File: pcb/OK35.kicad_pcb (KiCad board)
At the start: 2 copper layers, 133.3 x 116.2 mm, 78 parts, among them SW1 SW_SPST, SW10 SW_SPST, SW11 SW_SPST, SW12 SW_SPST, SW13 SW_SPST, SW14 SW_SPST, SW15 SW_SPST, SW16 SW_SPST, SW17 SW_SPST, SW18 SW_SPST, SW19 SW_SPST, SW2 SW_SPST, SW20 SW_SPST, SW21 SW_SPST, SW22 SW_SPST, SW23 SW_SPST, SW24 SW_SPST, SW25 SW_SPST, SW26 SW_SPST, SW27 SW_SPST, SW28 SW_SPST, SW29 SW_SPST, SW3 SW_SPST, SW30 SW_SPST, SW31 SW_SPST, SW32 SW_SPST, SW33 SW_SPST, SW34 SW_SPST, SW35 SW_SPST, SW4 SW_SPST, SW5 SW_SPST, SW6 SW_SPST, SW7 SW_SPST, SW8 SW_SPST, SW9 SW_SPST, U1 TRRS, U2 ProMicro

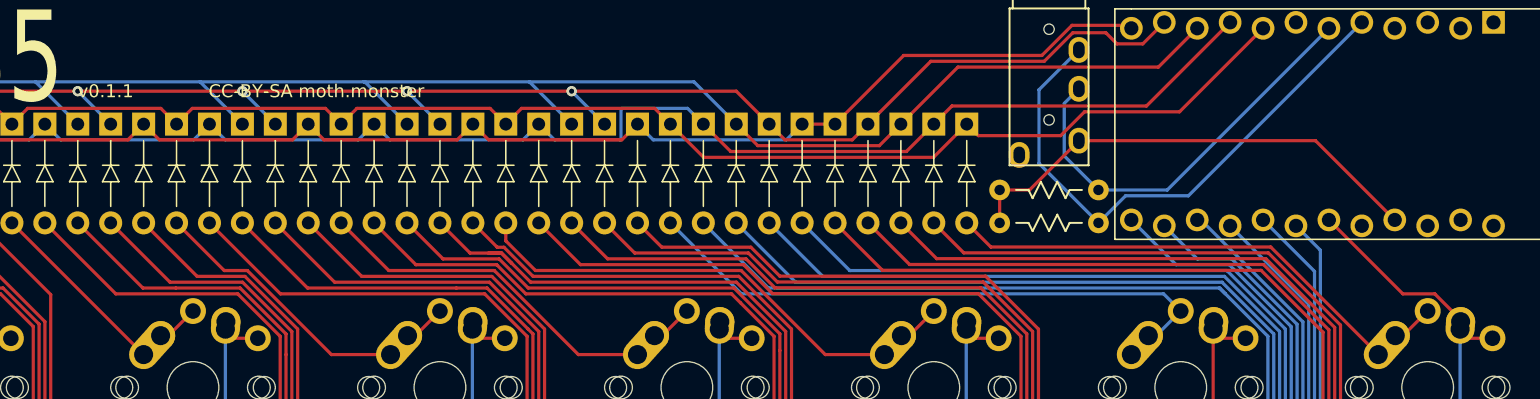
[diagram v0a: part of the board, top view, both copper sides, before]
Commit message: v0.1.2 - add handedness jumper
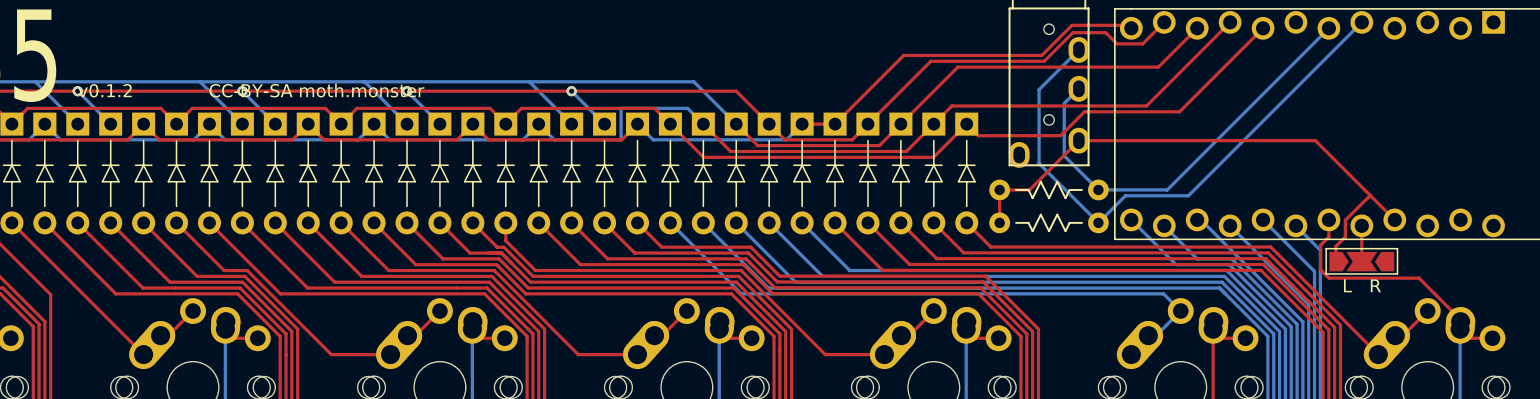
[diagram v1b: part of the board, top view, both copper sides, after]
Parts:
- added JP1: SolderJumper_3_Open, Jumper:SolderJumper-3_P2.0mm_Open_TrianglePad1.0x1.5mm, F.Cu at (198.1, 53.3)
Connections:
- D1 pad 1: Row1 -> Row0
- D10 pad 1: Row2 -> Row1
- D11 pad 1: Row2 -> Row1
- D12 pad 1: Row2 -> Row1
- D13 pad 1: Row2 -> Row1
- D14 pad 1: Row2 -> Row1
- D15 pad 1: Row3 -> Row2
- D16 pad 1: Row3 -> Row2
- D17 pad 1: Row3 -> Row2
- D18 pad 1: Row3 -> Row2
- D19 pad 1: Row3 -> Row2
- D2 pad 1: Row1 -> Row0
- D20 pad 1: Row3 -> Row2
- D21 pad 1: Row3 -> Row2
- D22 pad 1: Row4 -> Row3
- D23 pad 1: Row4 -> Row3
- D24 pad 1: Row4 -> Row3
- D25 pad 1: Row4 -> Row3
- D26 pad 1: Row4 -> Row3
- D27 pad 1: Row4 -> Row3
- D28 pad 1: Row4 -> Row3
- D29 pad 1: Row5 -> Row4
- D3 pad 1: Row1 -> Row0
- D30 pad 1: Row5 -> Row4
- D31 pad 1: Row5 -> Row4
- D32 pad 1: Row5 -> Row4
- D33 pad 1: Row5 -> Row4
- D34 pad 1: Row5 -> Row4
- D35 pad 1: Row5 -> Row4
- D4 pad 1: Row1 -> Row0
- D5 pad 1: Row1 -> Row0
- D6 pad 1: Row1 -> Row0
- D7 pad 1: Row1 -> Row0
- D8 pad 1: Row2 -> Row1
- D9 pad 1: Row2 -> Row1
- SW1 pad 1: Col1 -> Col0
- SW10 pad 1: Col3 -> Col2
- SW11 pad 1: Col4 -> Col3
- SW12 pad 1: Col5 -> Col4
- SW13 pad 1: Col6 -> Col5
- SW14 pad 1: Col7 -> Col6
- SW15 pad 1: Col1 -> Col0
- SW16 pad 1: Col2 -> Col1
- SW17 pad 1: Col3 -> Col2
- SW18 pad 1: Col4 -> Col3
- SW19 pad 1: Col5 -> Col4
- SW2 pad 1: Col2 -> Col1
- SW20 pad 1: Col6 -> Col5
- SW21 pad 1: Col7 -> Col6
- SW22 pad 1: Col1 -> Col0
- SW23 pad 1: Col2 -> Col1
- SW24 pad 1: Col3 -> Col2
- SW25 pad 1: Col4 -> Col3
- SW26 pad 1: Col5 -> Col4
- SW27 pad 1: Col6 -> Col5
- SW28 pad 1: Col7 -> Col6
- SW29 pad 1: Col1 -> Col0
- SW3 pad 1: Col3 -> Col2
- SW30 pad 1: Col2 -> Col1
- SW31 pad 1: Col3 -> Col2
- SW32 pad 1: Col4 -> Col3
- SW33 pad 1: Col5 -> Col4
- SW34 pad 1: Col6 -> Col5
- SW35 pad 1: Col7 -> Col6
- SW4 pad 1: Col4 -> Col3
- SW5 pad 1: Col5 -> Col4
- SW6 pad 1: Col6 -> Col5
- SW7 pad 1: Col7 -> Col6
- SW8 pad 1: Col1 -> Col0
- SW9 pad 1: Col2 -> Col1
- U2 pad 10: Row3 -> Row2
- U2 pad 11: Row4 -> Row3
- U2 pad 12: Row5 -> Row4
- U2 pad 13: Col6 -> Col5
- U2 pad 14: Col5 -> Col4
- U2 pad 15: Col4 -> Col3
- U2 pad 16: Col3 -> Col2
- U2 pad 17: Col2 -> Col1
- U2 pad 18: Col1 -> Col0
- U2 pad 19: Col7 -> Col6
- U2 pad 20: unconnected-(U2-Pad20) -> Net-(U2-Pad20)
- U2 pad 8: Row1 -> Row0
- U2 pad 9: Row2 -> Row1
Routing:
- net Col0: track 0.00 -> 291.2 mm
- net Row0: track 0.00 -> 120.2 mm
- net Col7: track 103.7 -> 0.00 mm
- net Row5: track 97.2 -> 0.00 mm
- net Col6: track 187.3 -> 106.9 mm
- net Col5: track 212.9 -> 187.3 mm
- net Col3: track 253.0 -> 231.1 mm
- net Col1: track 291.2 -> 271.9 mm
- net Col2: track 271.9 -> 253.0 mm
- net Row4: track 115.4 -> 97.2 mm, vias 5 -> 0
- net Col4: track 231.1 -> 212.9 mm
- net Row3: track 124.7 -> 115.4 mm, vias 0 -> 5
- net Row2: track 116.5 -> 124.7 mm
- net VCC: track 37.1 -> 43.3 mm
- net Row1: track 120.2 -> 116.5 mm
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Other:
- board text added: "L R"
- board text added: "v0.1.2"
- board text removed: "v0.1.1"

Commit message: v0.1.2 finalized public release
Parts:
- moved D1 0.19 mm to (86.4, 46.4)
- moved D10 0.19 mm to (114.3, 46.4)
- moved D11 0.19 mm to (127.0, 46.4)
- moved D12 0.19 mm to (139.7, 46.4)
- moved D13 0.19 mm to (152.4, 46.4)
- moved D14 0.19 mm to (170.2, 46.4)
- moved D15 0.19 mm to (91.4, 46.4)
- moved D16 0.19 mm to (104.1, 46.4)
- moved D17 0.19 mm to (116.8, 46.4)
- moved D18 0.19 mm to (129.5, 46.4)
- moved D19 0.19 mm to (142.2, 46.4)
- moved D2 0.19 mm to (99.1, 46.4)
- moved D20 0.19 mm to (154.9, 46.4)
- moved D21 0.19 mm to (167.6, 46.4)
- moved D22 0.19 mm to (94.0, 46.4)
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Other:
- board text added: "Good order number hiding spot Nobody thinks to look under the MCU!"
- board text added: "If you order your own batch, put something creative and/or funny here"
- board text added: "JLCJLCJLCJLC"
- board text added: "OK35 v0.1.2 CC-BY-SA moth.monster"
- board text removed: "CC-BY-SA moth.monster"
- board text removed: "OK35"
- board text removed: "v0.1.2"
